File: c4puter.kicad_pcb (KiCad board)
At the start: 6 copper layers, 200 x 200 mm, 34 parts, among them J1 CONN-10018783-10202TLF-PCIEx8, J2 CONN-10018783-10202TLF-PCIEx8, J3 CONN-10018783-10202TLF-PCIEx8, J4 CONN-10018783-10202TLF-PCIEx8, J5 CONN-10018783-10202TLF-PCIEx8, J6 CONN-10018783-10202TLF-PCIEx8, J7 19V 3A, J8 DEBUG, U1 AOZ1037, U2 TSC101B

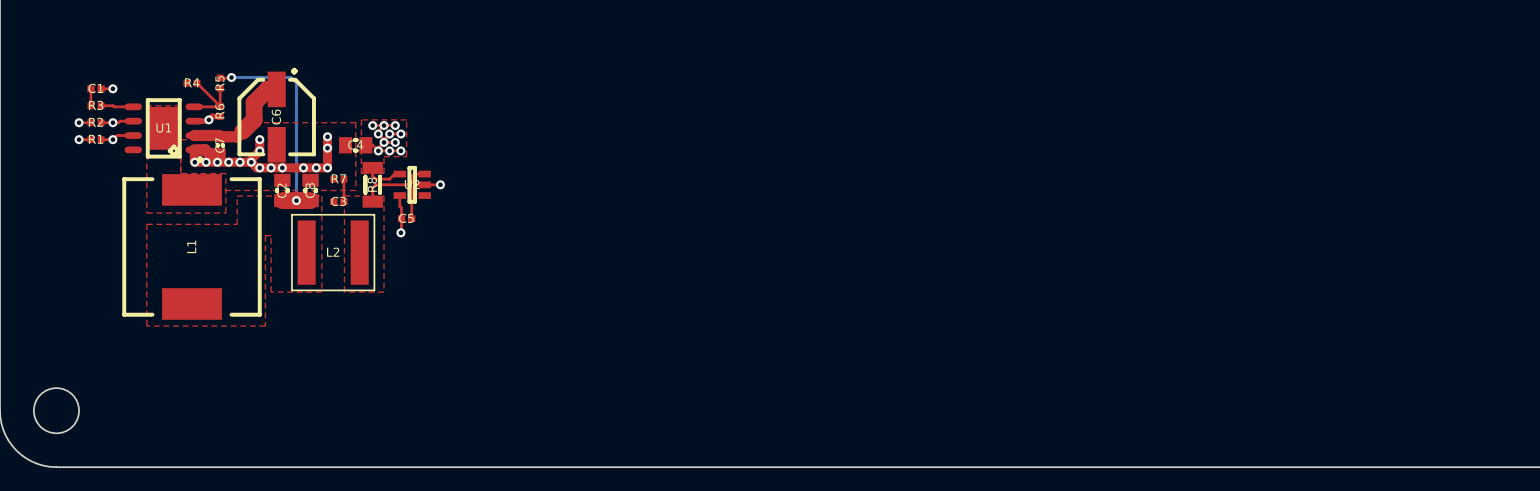
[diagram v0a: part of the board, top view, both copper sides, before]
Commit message: Finish power supplies
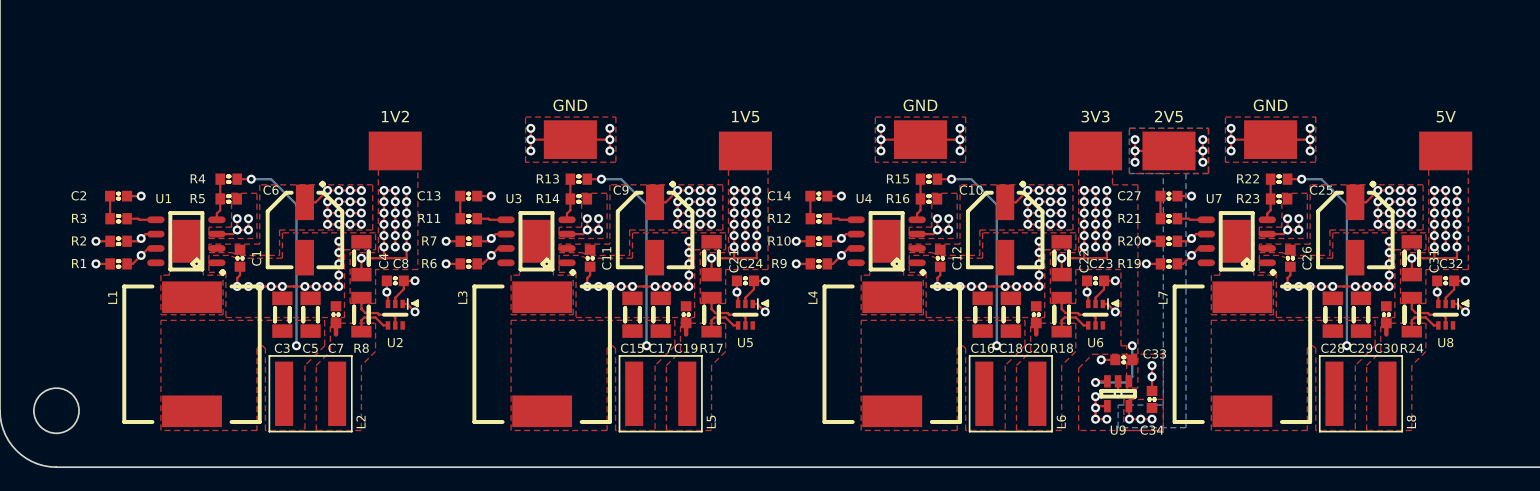
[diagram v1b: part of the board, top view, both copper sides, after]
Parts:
- added C10: 22u(P), IPC7351-Nominal:CAPAE660X570, F.Cu at (89.0, 179.0)
- added C11: 100n, IPC7351-Nominal:CAPC1608X55, F.Cu at (52.2, 181.5)
- added C12: 100n, IPC7351-Nominal:CAPC1608X55, F.Cu at (83.2, 181.5)
- added C13: 220p, IPC7351-Nominal:CAPC1608X55, F.Cu at (41.5, 176.0)
- added C14: 220p, IPC7351-Nominal:CAPC1608X55, F.Cu at (72.5, 176.0)
- added C15: 22u, IPC7351-Nominal:CAPC3216X70, F.Cu at (56.0, 186.5)
- added C16: 22u, IPC7351-Nominal:CAPC3216X70, F.Cu at (87.0, 186.5)
- added C17: 22u, IPC7351-Nominal:CAPC3216X70, F.Cu at (58.5, 186.5)
- added C18: 22u, IPC7351-Nominal:CAPC3216X70, F.Cu at (89.5, 186.5)
- added C19: 100n, IPC7351-Nominal:CAPC1608X55, F.Cu at (60.8, 186.5)
- added C20: 100n, IPC7351-Nominal:CAPC1608X55, F.Cu at (91.8, 186.5)
- added C21: 22u, IPC7351-Nominal:CAPC3216X70, F.Cu at (63.0, 181.5)
- added C22: 22u, IPC7351-Nominal:CAPC3216X70, F.Cu at (94.0, 181.5)
- added C23: 100n, IPC7351-Nominal:CAPC1608X55, F.Cu at (97.0, 183.5)
- added C24: 100n, IPC7351-Nominal:CAPC1608X55, F.Cu at (66.0, 183.5)
- added C25: 22u(P), IPC7351-Nominal:CAPAE660X570, F.Cu at (120.0, 179.0)
- added C26: 100n, IPC7351-Nominal:CAPC1608X55, F.Cu at (114.2, 181.5)
- added C27: 220p, IPC7351-Nominal:CAPC1608X55, F.Cu at (103.5, 176.0)
- added C28: 22u, IPC7351-Nominal:CAPC3216X70, F.Cu at (118.0, 186.5)
- added C29: 22u, IPC7351-Nominal:CAPC3216X70, F.Cu at (120.5, 186.5)
- added C30: 100n, IPC7351-Nominal:CAPC1608X55, F.Cu at (122.8, 186.5)
- added C31: 22u, IPC7351-Nominal:CAPC3216X70, F.Cu at (125.0, 181.5)
- added C32: 100n, IPC7351-Nominal:CAPC1608X55, F.Cu at (128.0, 183.5)
- added C33: 2u2, IPC7351-Nominal:CAPC1608X55, F.Cu at (99.5, 190.5)
- added C34: 2u2, IPC7351-Nominal:CAPC1608X55, F.Cu at (102.0, 194.0)
- added C9: 22u(P), IPC7351-Nominal:CAPAE660X570, F.Cu at (58.0, 179.0)
- added L3: 4u7, manuf:BOURNS-SRR1210, F.Cu at (48.0, 190.0)
- added L4: 10u, manuf:BOURNS-SRR1210, F.Cu at (79.0, 190.0)
- added L5: 2u2, manuf:MURATA-DG6050C, F.Cu at (58.5, 193.5)
- added L6: 2u2, manuf:MURATA-DG6050C, F.Cu at (89.5, 193.5)
- added L7: 10u, manuf:BOURNS-SRR1210, F.Cu at (110.0, 190.0)
- added L8: 2u2, manuf:MURATA-DG6050C, F.Cu at (120.5, 193.5)
- added R10: 100k, IPC7351-Nominal:RESC1608X50, F.Cu at (72.5, 180.0)
- added R11: 10k, IPC7351-Nominal:RESC1608X50, F.Cu at (41.5, 178.0)
- added R12: 10k, IPC7351-Nominal:RESC1608X50, F.Cu at (72.5, 178.0)
- added R13: 10k, IPC7351-Nominal:RESC1608X50, F.Cu at (51.2, 174.5)
- added R14: 10k, IPC7351-Nominal:RESC1608X50, F.Cu at (51.2, 176.2)
- added R15: 10k, IPC7351-Nominal:RESC1608X50, F.Cu at (82.2, 174.5)
- added R16: 10k, IPC7351-Nominal:RESC1608X50, F.Cu at (82.2, 176.2)
- added R17: 0R005, IPC7351-Nominal:RESC3216X60, F.Cu at (63.0, 186.5)
- added R18: 0R005, IPC7351-Nominal:RESC3216X60, F.Cu at (94.0, 186.5)
- added R19: 100k, IPC7351-Nominal:RESC1608X50, F.Cu at (103.5, 182.0)
- added R20: 100k, IPC7351-Nominal:RESC1608X50, F.Cu at (103.5, 180.0)
- added R21: 10k, IPC7351-Nominal:RESC1608X50, F.Cu at (103.5, 178.0)
- added R22: 10k, IPC7351-Nominal:RESC1608X50, F.Cu at (113.2, 174.5)
- added R23: 10k, IPC7351-Nominal:RESC1608X50, F.Cu at (113.2, 176.2)
- added R24: 0R005, IPC7351-Nominal:RESC3216X60, F.Cu at (125.0, 186.5)
- added R9: 100k, IPC7351-Nominal:RESC1608X50, F.Cu at (72.5, 182.0)
- added TP1: 1V2, manuf:TESTPOINT-KEYSTONE-5018, F.Cu at (35.0, 172.0)
- added TP2: 3V3, manuf:TESTPOINT-KEYSTONE-5018, F.Cu at (97.0, 172.0)
- added TP3: 1V5, manuf:TESTPOINT-KEYSTONE-5018, F.Cu at (66.0, 172.0)
- added TP4: 5V, manuf:TESTPOINT-KEYSTONE-5018, F.Cu at (128.0, 172.0)
- added TP5: 2V5, manuf:TESTPOINT-KEYSTONE-5018, F.Cu at (103.5, 172.0)
- added TP6: GND, manuf:TESTPOINT-KEYSTONE-5018, F.Cu at (50.5, 171.0)
- added TP7: GND, manuf:TESTPOINT-KEYSTONE-5018, F.Cu at (81.5, 171.0)
- added TP8: GND, manuf:TESTPOINT-KEYSTONE-5018, F.Cu at (112.5, 171.0)
- added U3: AOZ1037, IPC7351-Nominal:SOIC127P600X175-9, F.Cu at (47.5, 180.0)
- added U4: AOZ1037, IPC7351-Nominal:SOIC127P600X175-9, F.Cu at (78.5, 180.0)
- added U5: INA199, smd-semi:SC-70-6, F.Cu at (66.0, 186.5)
- added U6: INA199, smd-semi:SC-70-6, F.Cu at (97.0, 186.5)
- added U7: AOZ1037, IPC7351-Nominal:SOIC127P600X175-9, F.Cu at (109.5, 180.0)
- added U8: INA199, smd-semi:SC-70-6, F.Cu at (128.0, 186.5)
- added U9: TLV70225DBV, smd-semi:SOT-23-5, F.Cu at (99.0, 193.5)
- C1: value 220p -> 100n; footprint IPC7351-Nominal:CAPC1005X55 -> IPC7351-Nominal:CAPC1608X55
- C2: value 22u -> 220p; footprint IPC7351-Nominal:CAPC2012X70 -> IPC7351-Nominal:CAPC1608X55
- C3, C5: value 100n -> 22u; footprint IPC7351-Nominal:CAPC1005X55 -> IPC7351-Nominal:CAPC3216X70
- C4: footprint IPC7351-Nominal:CAPC2012X70 -> IPC7351-Nominal:CAPC3216X70
- C8: value 22u -> 100n; footprint IPC7351-Nominal:CAPC2012X70 -> IPC7351-Nominal:CAPC1608X55
- R1, R2, R3, R6: footprint IPC7351-Nominal:RESC1005X40 -> IPC7351-Nominal:RESC1608X50
- R4, R5: value 100k -> 10k; footprint IPC7351-Nominal:RESC1005X40 -> IPC7351-Nominal:RESC1608X50
- R7: value 47 -> 100k; footprint IPC7351-Nominal:RESC1005X40 -> IPC7351-Nominal:RESC1608X50
- R8: value 0R01 -> 0R005
- U2: value TSC101B -> INA199; footprint smd-semi:SOT-23-5 -> smd-semi:SC-70-6
- moved R6 25.8 mm to (41.5, 182.0), turned to 0 degrees
- moved C1 19.7 mm to (21.2, 181.5), turned to 270 degrees
- moved C7 18.2 mm to (29.8, 186.5), turned to 90 degrees
- moved C2 14.5 mm to (10.5, 176.0), turned to 0 degrees
- moved R7 12.7 mm to (41.5, 180.0), turned to 180 degrees
- moved L2 12.7 mm to (27.5, 193.5)
- moved C5 12.0 mm to (27.5, 186.5), turned to 90 degrees
- moved U2 11.6 mm to (35.0, 186.5), turned to 270 degrees
- moved R8 11.5 mm to (32.0, 186.5)
- moved C3 11.2 mm to (25.0, 186.5), turned to 90 degrees
- moved R1 11.2 mm to (10.5, 182.0), turned to 0 degrees
- moved C8 11.0 mm to (35.0, 183.5), turned to 0 degrees
- moved R2 10.7 mm to (10.5, 180.0), turned to 180 degrees
- moved C6 10.3 mm to (27.0, 179.0)
- moved R5 10.3 mm to (20.2, 176.2), turned to 180 degrees
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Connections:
- C1 pad 1: Net-(C1-Pad1) -> +12
- C2 pad 1: /Power/RAW1V2 -> Net-(C2-Pad1)
- C3 pad 1: Net-(C3-Pad1) -> /Power/RAW1V2
- C3 pad 2: /Power/S+1V2 -> GND
- C5 pad 1: GND -> /Power/RAW1V2
- C5 pad 2: +3.3SB -> GND
- C7 pad 1: +12 -> /Power/S+1V2
- C8 pad 1: /Power/RAW1V2 -> +3.3SB
- R1 pad 1: /Power/PG1V2 -> +3.3SB
- R1 pad 2: +3.3SB -> /Power/PG1V2
- R2 pad 1: GND -> /Power/EN1V2
- R2 pad 2: /Power/EN1V2 -> GND
- R3 pad 2: Net-(C1-Pad1) -> Net-(C2-Pad1)
- R4 pad 1: /Power/TRIM1V2 -> Net-(R4-Pad1)
- R4 pad 2: Net-(R4-Pad2) -> /Power/RAW1V2
- R5 pad 1: Net-(R4-Pad2) -> GND
- R5 pad 2: /Power/RAW1V2 -> Net-(R4-Pad1)
- R6 pad 1: GND -> +3.3SB
- R6 pad 2: Net-(R4-Pad2) -> /Power/PG1V5
- R7 pad 1: GND -> /Power/EN1V5
- R7 pad 2: Net-(C3-Pad1) -> GND
- U1 pad 4: Net-(R4-Pad2) -> Net-(R4-Pad1)
- U2 pad 1: /Power/IMON1V2 -> GND
- U2 pad 3: /Power/S+1V2 -> +3.3SB
- U2 pad 4: /Power/1V2 -> /Power/S+1V2
- U2 pad 5: +3.3SB -> /Power/1V2
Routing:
- net GND: track 609.4 -> 729.4 mm, vias 57 -> 147
- net +12: track 9.97 -> 69.7 mm, vias 0 -> 64
- net /Power/3V3: track 0.00 -> 35.8 mm, vias 0 -> 21
- net /Power/1V5: track 0.00 -> 28.5 mm, vias 0 -> 19
- net /Power/5V: track 0.00 -> 28.5 mm, vias 0 -> 19
- net /Power/RAW5V: track 0.00 -> 18.7 mm, vias 0 -> 2
- net /Power/RAW3V3: track 0.00 -> 18.7 mm, vias 0 -> 2
- net /Power/RAW1V5: track 0.00 -> 18.7 mm, vias 0 -> 2
- net /Power/1V2: track 14.3 -> 28.5 mm, vias 11 -> 19
- net /Power/2V5: track 0.00 -> 13.2 mm, vias 0 -> 9
- net +3.3SB: track 4.43 -> 13.4 mm, vias 2 -> 8
- net Net-(R4-Pad2): track 6.82 -> 0.00 mm
- net /Power/S+5V: track 0.00 -> 4.74 mm
- net /Power/S+3V3: track 0.00 -> 4.74 mm
- net /Power/S+1V5: track 0.00 -> 4.74 mm
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- added copper zone on F.Cu, net +12
- added copper zone on F.Cu, net /Power/1V5
- added copper zone on B.Cu, net /Power/2V5
- added copper zone on F.Cu, net /Power/2V5
- added copper zone on F.Cu, net /Power/3V3
- added copper zone on F.Cu, net /Power/5V
- added copper zone on F.Cu, net /Power/RAW1V5
- added copper zone on F.Cu, net /Power/RAW3V3
- added copper zone on F.Cu, net /Power/RAW5V
- added copper zone on F.Cu, net /Power/S+1V5
- added copper zone on F.Cu, net /Power/S+3V3
- added copper zone on F.Cu, net /Power/S+5V
- added copper zone on F.Cu, net /Power/SW1V5
- added copper zone on F.Cu, net /Power/SW3V3
- added copper zone on F.Cu, net /Power/SW5V
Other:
- net class Default: clearance 0.1016 -> 0.2; trace_width 0.1016 -> 0.2; via_dia 0.48 -> 0.8; via_drill 0.2 -> 0.4
- net class Tight added: clearance 0.1016, trace_width 0.1016, via_dia 0.48, via_drill 0.2
- rule trace_clearance: 0.1016 -> 0.2

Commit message: Upgrade FPGA size, re-route SDRAM
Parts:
- removed J5, J6: CONN-10018783-10202TLF-PCIEx8, conn-fci:CONN-10018783-10202TLF-PCIEx8-FCI
- BRIDGE1: value XC6SLX25-CSG324 -> XC6SLX25-FGG484; footprint manuf:XILINX-CSG324 -> manuf:XILINX-FGG484
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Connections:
- net /Multibridge/CPU4 renamed Net-(BRIDGE1-PadU15)
- net /Multibridge/CPU5 renamed Net-(BRIDGE1-PadV15)
- BRIDGE1 pad A10: /Multibridge/DQ56 -> /Multibridge/DQS4_N
- BRIDGE1 pad A11: /Multibridge/DM7 -> /Multibridge/DQS5_N
- BRIDGE1 pad A12: /Multibridge/DQ59 -> /Multibridge/DQ35
- BRIDGE1 pad A13: /Multibridge/SA1 -> VDDRREF
- BRIDGE1 pad A14: VREF -> /Multibridge/DQ41
- BRIDGE1 pad A15: Net-(BRIDGE1-PadA15) -> /Multibridge/DQ42
- BRIDGE1 pad A16: Net-(BRIDGE1-PadA16) -> /Multibridge/DQ43
- BRIDGE1 pad A17: /Power Distrib/BR_TCK -> /Multibridge/DQ49
- BRIDGE1 pad A18: GND -> /Multibridge/DQS6_N
- BRIDGE1 pad A2: /Multibridge/DQS4_N -> /Multibridge/A10
- BRIDGE1 pad A3: /Multibridge/DQ34 -> /Multibridge/~WE
- BRIDGE1 pad A4: /Multibridge/DQ40 -> VDDRREF
- BRIDGE1 pad A5: /Multibridge/DM5 -> /Multibridge/~CAS
- BRIDGE1 pad A6: VREF -> /Multibridge/~S1
- BRIDGE1 pad A7: /Multibridge/DQ48 -> /Multibridge/DQ32
- BRIDGE1 pad A8: /Multibridge/DQS6_N -> Net-(BRIDGE1-PadA8)
- BRIDGE1 pad A9: /Multibridge/DQ50 -> VDDRREF
- BRIDGE1 pad B1: +3.3 -> /Multibridge/CK0_N
- BRIDGE1 pad B10: +1.5 -> /Multibridge/DQS4_P
- BRIDGE1 pad B11: /Multibridge/DQ58 -> VRAM
- BRIDGE1 pad B12: /Multibridge/SA0 -> /Multibridge/DQ40
- BRIDGE1 pad B14: /Multibridge/DQ63 -> /Multibridge/DM5
- BRIDGE1 pad B15: +1.5 -> VRAM
- BRIDGE1 pad B16: Net-(BRIDGE1-PadB16) -> /Multibridge/DQ48
- BRIDGE1 pad B17: +3.3 -> GND
- BRIDGE1 pad B18: /Power Distrib/BR_TMS -> /Multibridge/DQS6_P
- BRIDGE1 pad B2: /Multibridge/DQS4_P -> /Multibridge/CK0_P
- BRIDGE1 pad B3: /Multibridge/DQ35 -> VDDRREF
- BRIDGE1 pad B4: /Multibridge/DQ41 -> VRAM
- BRIDGE1 pad B5: +1.5 -> GND
- BRIDGE1 pad B6: /Multibridge/DQ43 -> /Multibridge/A13
- BRIDGE1 pad B7: GND -> VRAM
- BRIDGE1 pad B8: /Multibridge/DQS6_P -> /Multibridge/DQ33
- BRIDGE1 pad B9: /Multibridge/DQ51 -> GND
- BRIDGE1 pad C1: VREF -> /Multibridge/CK1_N
- BRIDGE1 pad C10: /Multibridge/DQ57 -> /Multibridge/DQ44
- BRIDGE1 pad C11: /Multibridge/DQ54 -> /Multibridge/DQS5_P
- BRIDGE1 pad C12: /Multibridge/DQ60 -> /Multibridge/DQ46
- BRIDGE1 pad C14: /Multibridge/DQS7_N -> /Multibridge/DQ52
- BRIDGE1 pad C15: /Multibridge/DQ62 -> /Multibridge/DM6
- BRIDGE1 pad C16: GND -> VDDRREF
- BRIDGE1 pad C17: /Multibridge/CD2 -> /Multibridge/DQ55
- BRIDGE1 pad C18: /Multibridge/CD3 -> /Power Distrib/BR_TMS
- BRIDGE1 pad C2: /Multibridge/DQ33 -> VRAM
- BRIDGE1 pad C3: GND -> /Multibridge/CK1_P
- BRIDGE1 pad C4: VREF -> (no net)
- BRIDGE1 pad C5: /Multibridge/DQ42 -> /Multibridge/BA1
- BRIDGE1 pad C6: Net-(BRIDGE1-PadC6) -> /Multibridge/~RAS
- BRIDGE1 pad C7: /Multibridge/DQ49 -> /Multibridge/ODT0
- BRIDGE1 pad C8: /Multibridge/DQ44 -> /Multibridge/DQ36
- BRIDGE1 pad C9: /Multibridge/DQS5_N -> /Multibridge/DM4
- BRIDGE1 pad D1: /Multibridge/~S1 -> /Multibridge/A3
- BRIDGE1 pad D10: GND -> /Multibridge/DQ45
- BRIDGE1 pad D11: Net-(BRIDGE1-PadD11) -> /Multibridge/DQ34
- BRIDGE1 pad D12: /Multibridge/DQ61 -> /Multibridge/DQ47
- BRIDGE1 pad D13: +1.5 -> /Multibridge/DQS7_N
- BRIDGE1 pad D14: /Multibridge/DQS7_P -> /Multibridge/DQ53
- BRIDGE1 pad D15: /Power Distrib/BR_TDI -> /Multibridge/DQ54
- BRIDGE1 pad D16: /Power Distrib/BR_TDO -> VCCAUX
- BRIDGE1 pad D17: /Multibridge/CD6 -> /Multibridge/DQ60
- BRIDGE1 pad D18: /Multibridge/CD7 -> GND
- BRIDGE1 pad D2: /Multibridge/DQ32 -> /Multibridge/A1
- BRIDGE1 pad D3: /Multibridge/ODT0 -> (no net)
- BRIDGE1 pad D4: /Multibridge/ODT1 -> GND
- BRIDGE1 pad D5: GND -> (no net)
- BRIDGE1 pad D6: /Multibridge/DQ38 -> /Multibridge/~S0
- BRIDGE1 pad D7: +1.5 -> /Multibridge/ODT1
- BRIDGE1 pad D8: /Multibridge/DQ39 -> /Multibridge/DQ37
- BRIDGE1 pad D9: /Multibridge/DQS5_P -> /Multibridge/DQ38
- BRIDGE1 pad E1: /Multibridge/~CAS -> /Multibridge/A5
- BRIDGE1 pad E10: +1.5 -> (no net)
- BRIDGE1 pad E11: Net-(BRIDGE1-PadE11) -> GND
- BRIDGE1 pad E12: /Multibridge/DM6 -> Net-(BRIDGE1-PadE12)
- BRIDGE1 pad E13: /Multibridge/DQ55 -> VRAM
- BRIDGE1 pad E14: +3.3 -> /Multibridge/DM7
- BRIDGE1 pad E16: /Multibridge/CD10 -> /Multibridge/DQ63
- BRIDGE1 pad E17: Net-(BRIDGE1-PadE17) -> VRAM
- BRIDGE1 pad E18: /Multibridge/CD11 -> /Power Distrib/BR_TDI
- BRIDGE1 pad E2: +1.5 -> GND
- BRIDGE1 pad E3: /Multibridge/A13 -> /Multibridge/A0
- BRIDGE1 pad E4: /Multibridge/~RAS -> (no net)
- BRIDGE1 pad E5: +3.3 -> (no net)
- BRIDGE1 pad E6: Net-(BRIDGE1-PadE6) -> (no net)
- BRIDGE1 pad E7: Net-(BRIDGE1-PadE7) -> GND
- BRIDGE1 pad E8: Net-(BRIDGE1-PadE8) -> (no net)
- BRIDGE1 pad E9: +3.3 -> VRAM
- BRIDGE1 pad F1: /Multibridge/A10 -> /Multibridge/A9
- BRIDGE1 pad F10: /Multibridge/DQ46 -> (no net)
- BRIDGE1 pad F11: /Multibridge/DQ52 -> VCCAUX
- BRIDGE1 pad F12: /Multibridge/DQ53 -> /Multibridge/DQ61
- BRIDGE1 pad F13: Net-(BRIDGE1-PadF13) -> /Multibridge/DQS7_P
- BRIDGE1 pad F14: /Multibridge/CD4 -> /Multibridge/DQ59
- BRIDGE1 pad F15: /Multibridge/CD0 -> /Multibridge/SA0
- BRIDGE1 pad F16: /Multibridge/CD1 -> (no net)
- BRIDGE1 pad F17: /Multibridge/CD14 -> (no net)
- BRIDGE1 pad F18: /Multibridge/CD15 -> Net-(BRIDGE1-PadF18)
- BRIDGE1 pad F2: /Multibridge/~WE -> /Multibridge/A8
- BRIDGE1 pad F3: /Multibridge/BA1 -> /Multibridge/A2
- BRIDGE1 pad F4: /Multibridge/~S0 -> VRAM
- BRIDGE1 pad F5: /Multibridge/DQ36 -> /Multibridge/DQ50
- BRIDGE1 pad F6: /Multibridge/DQ37 -> VRAM
- BRIDGE1 pad F7: Net-(BRIDGE1-PadF7) -> (no net)
- BRIDGE1 pad F8: Net-(BRIDGE1-PadF8) -> (no net)
- BRIDGE1 pad F9: VREF -> (no net)
- BRIDGE1 pad G1: /Multibridge/CK0_N -> /Multibridge/A12
- BRIDGE1 pad G10: +3.3 -> VRAM
- BRIDGE1 pad G11: /Multibridge/DQ47 -> (no net)
- BRIDGE1 pad G12: GND -> VCCAUX
- BRIDGE1 pad G13: /Multibridge/CD9 -> /Multibridge/DQ58
- BRIDGE1 pad G14: /Multibridge/CD5 -> VRAM
- BRIDGE1 pad G15: Net-(BRIDGE1-PadG15) -> /Power Distrib/BR_TCK
- BRIDGE1 pad G16: /Multibridge/CD20 -> (no net)
- BRIDGE1 pad G17: GND -> (no net)
- BRIDGE1 pad G18: /Multibridge/CD21 -> GND
- BRIDGE1 pad G2: GND -> VRAM
- BRIDGE1 pad G3: /Multibridge/CK0_P -> /Multibridge/A6
- BRIDGE1 pad G4: +1.5 -> /Multibridge/A4
- BRIDGE1 pad G6: /Multibridge/DM4 -> /Multibridge/DQ51
- BRIDGE1 pad G7: +1.2 -> (no net)
- BRIDGE1 pad G8: Net-(BRIDGE1-PadG8) -> (no net)
- BRIDGE1 pad G9: /Multibridge/DQ45 -> (no net)
- BRIDGE1 pad H1: /Multibridge/A1 -> /Multibridge/CKE0
- BRIDGE1 pad H10: GND -> (no net)
- BRIDGE1 pad H11: +1.2 -> (no net)
- BRIDGE1 pad H12: /Multibridge/CD8 -> /Multibridge/DQ56
- BRIDGE1 pad H13: /Multibridge/CD16 -> /Multibridge/DQ62
- BRIDGE1 pad H14: /Multibridge/CD17 -> /Multibridge/SA1
- BRIDGE1 pad H15: /Multibridge/CD18 -> VCCAUX
- BRIDGE1 pad H16: /Multibridge/CD19 -> (no net)
- BRIDGE1 pad H17: /Multibridge/CD30 -> (no net)
- BRIDGE1 pad H18: /Multibridge/CD31 -> Net-(BRIDGE1-PadH18)
- BRIDGE1 pad H2: /Multibridge/A3 -> /Multibridge/BA2
- BRIDGE1 pad H3: /Multibridge/CK1_N -> /Multibridge/A11
- BRIDGE1 pad H4: /Multibridge/CK1_P -> /Multibridge/A7
- BRIDGE1 pad H5: /Multibridge/A0 -> /Multibridge/DQ7
- BRIDGE1 pad H6: /Multibridge/A2 -> /Multibridge/DQ12
- BRIDGE1 pad H7: Net-(BRIDGE1-PadH7) -> GND
- BRIDGE1 pad H8: GND -> /Multibridge/DQ13
- BRIDGE1 pad H9: +1.2 -> VCCAUX
- BRIDGE1 pad J1: /Multibridge/A5 -> /Multibridge/DQ27
- BRIDGE1 pad J10: +1.2 -> VCORE
- BRIDGE1 pad J12: +3.3 -> VCORE
- BRIDGE1 pad J13: /Multibridge/CD22 -> GND
- BRIDGE1 pad J14: Net-(BRIDGE1-PadJ14) -> VCORE
- BRIDGE1 pad J16: /Multibridge/CD_CLK -> (no net)
- BRIDGE1 pad J18: /Multibridge/CD_~ADH -> VCCO1
- BRIDGE1 pad J2: +1.5 -> GND
- BRIDGE1 pad J3: /Multibridge/A8 -> /Multibridge/A15
- BRIDGE1 pad J4: GND -> /Multibridge/A14
- BRIDGE1 pad J5: +1.5 -> VRAM
- BRIDGE1 pad J6: /Multibridge/A4 -> /Multibridge/DQS0_N
- BRIDGE1 pad J7: Net-(BRIDGE1-PadJ7) -> /Multibridge/DQ6
- BRIDGE1 pad J8: +1.2 -> VCORE
- BRIDGE1 pad K1: /Multibridge/A9 -> /Multibridge/DM3
- BRIDGE1 pad K11: +1.2 -> VCORE
- BRIDGE1 pad K12: /Multibridge/CD12 -> GND
- BRIDGE1 pad K13: /Multibridge/CD13 -> VCORE
- BRIDGE1 pad K14: /Multibridge/CD23 -> GND
- BRIDGE1 pad K15: /Multibridge/CD26 -> VCCAUX
- BRIDGE1 pad K16: /Multibridge/CD27 -> (no net)
- BRIDGE1 pad K17: /Multibridge/CD_~ADL -> Net-(BRIDGE1-PadK17)
- BRIDGE1 pad K18: /Multibridge/CD_R/~W -> Net-(BRIDGE1-PadK18)
- BRIDGE1 pad K2: /Multibridge/A12 -> /Multibridge/DQ26
- BRIDGE1 pad K3: /Multibridge/A6 -> /Multibridge/DQ31
- BRIDGE1 pad K4: /Multibridge/A7 -> /Multibridge/CKE1
- BRIDGE1 pad K5: /Multibridge/A11 -> /Multibridge/DQ5
- BRIDGE1 pad K6: Net-(BRIDGE1-PadK6) -> /Multibridge/DQS0_P
- BRIDGE1 pad K7: +3.3 -> (no net)
- BRIDGE1 pad K8: GND -> (no net)
- BRIDGE1 pad K9: +1.2 -> VCORE
- BRIDGE1 pad L1: /Multibridge/BA2 -> /Multibridge/DQ25
- BRIDGE1 pad L10: +1.2 -> VCORE
- BRIDGE1 pad L12: /Multibridge/CD24 -> VCORE
- BRIDGE1 pad L13: /Multibridge/CD25 -> GND
- BRIDGE1 pad L14: Net-(BRIDGE1-PadL14) -> VCORE
- BRIDGE1 pad L15: /Multibridge/CD28 -> (no net)
- BRIDGE1 pad L16: /Multibridge/CD29 -> VCCO1
- BRIDGE1 pad L17: /Multibridge/CD_SCLK -> Net-(BRIDGE1-PadL17)
- BRIDGE1 pad L18: /Multibridge/CD_MOSI -> GND
- BRIDGE1 pad L2: /Multibridge/CKE0 -> VRAM
- BRIDGE1 pad L3: /Multibridge/A14 -> /Multibridge/DQ30
- BRIDGE1 pad L4: /Multibridge/A15 -> /Multibridge/DQS3_N
- BRIDGE1 pad L5: Net-(BRIDGE1-PadL5) -> GND
- BRIDGE1 pad L6: Net-(BRIDGE1-PadL6) -> (no net)
- BRIDGE1 pad L7: Net-(BRIDGE1-PadL7) -> VRAM
- BRIDGE1 pad L8: +1.2 -> VCCAUX
- BRIDGE1 pad M1: /Multibridge/DQ27 -> /Multibridge/DQ19
- BRIDGE1 pad M10: /Multibridge/CPU14 -> GND
- BRIDGE1 pad M11: /Multibridge/CPU10 -> VCORE
- BRIDGE1 pad M12: +1.2 -> GND
- BRIDGE1 pad M13: Net-(BRIDGE1-PadM13) -> VCORE
- BRIDGE1 pad M14: Net-(BRIDGE1-PadM14) -> GND
- BRIDGE1 pad M15: Net-(BRIDGE1-PadM15) -> VCCAUX
- BRIDGE1 pad M16: /Multibridge/CD_MISO -> (no net)
- BRIDGE1 pad M17: GND -> (no net)
- BRIDGE1 pad M18: /Multibridge/CD_~SS0 -> (no net)
- BRIDGE1 pad M2: GND -> /Multibridge/DQ24
- BRIDGE1 pad M3: /Multibridge/CKE1 -> /Multibridge/DQS3_P
- BRIDGE1 pad M4: +1.5 -> VDDRREF
- BRIDGE1 pad M5: VREF -> /Multibridge/DQ28
- BRIDGE1 pad M6: GND -> (no net)
- BRIDGE1 pad M7: +1.2 -> (no net)
- BRIDGE1 pad M8: /Multibridge/CPUnW -> (no net)
- BRIDGE1 pad M9: +3.3 -> VCORE
- BRIDGE1 pad N1: /Multibridge/DQ26 -> /Multibridge/DQ18
- BRIDGE1 pad N10: /Multibridge/CPU13 -> VCORE
- BRIDGE1 pad N11: /Multibridge/CPU11 -> GND
- BRIDGE1 pad N12: /Multibridge/CPU8 -> VCORE
- BRIDGE1 pad N14: Net-(BRIDGE1-PadN14) -> VCORE
- BRIDGE1 pad N15: /Multibridge/CD_~SS5 -> /Power Distrib/BR_SUSP
- BRIDGE1 pad N16: Net-(BRIDGE1-PadN16) -> (no net)
- BRIDGE1 pad N17: /Multibridge/CD_~SS1 -> GND
- BRIDGE1 pad N18: /Multibridge/CD_~SS2 -> VCCO1
- BRIDGE1 pad N2: /Multibridge/DM3 -> GND
- BRIDGE1 pad N3: VREF -> /Multibridge/DQ29
- BRIDGE1 pad N4: /Multibridge/DQ31 -> (no net)
- BRIDGE1 pad N5: /Multibridge/DQ30 -> VRAM
- BRIDGE1 pad N6: /Multibridge/DQ15 -> (no net)
- BRIDGE1 pad N7: /Multibridge/CPUASTR -> (no net)
- BRIDGE1 pad N8: /Multibridge/CPUCLK -> VCCAUX
- BRIDGE1 pad N9: /Multibridge/CPU15 -> GND
- BRIDGE1 pad P1: /Multibridge/DQ25 -> /Multibridge/DQS2_N
- BRIDGE1 pad P10: +3.3 -> GND
- BRIDGE1 pad P11: /Multibridge/DQ6 -> VCORE
- BRIDGE1 pad P12: /Multibridge/CPU9 -> GND
- BRIDGE1 pad P13: Net-(BRIDGE1-PadP13) -> VCORE
- BRIDGE1 pad P14: +3.3 -> GND
- BRIDGE1 pad P15: Net-(BRIDGE1-PadP15) -> (no net)
- BRIDGE1 pad P16: Net-(BRIDGE1-PadP16) -> (no net)
- BRIDGE1 pad P17: /Multibridge/CD_~SS3 -> (no net)
- BRIDGE1 pad P18: /Multibridge/CD_~SS4 -> (no net)
- BRIDGE1 pad P2: /Multibridge/DQ24 -> /Multibridge/DQS2_P
- BRIDGE1 pad P3: Net-(BRIDGE1-PadP3) -> (no net)
- BRIDGE1 pad P4: Net-(BRIDGE1-PadP4) -> (no net)
- BRIDGE1 pad P5: +3.3 -> (no net)
- BRIDGE1 pad P6: /Multibridge/DQ23 -> (no net)
- BRIDGE1 pad P7: /Multibridge/DQ20 -> (no net)
- BRIDGE1 pad P8: /Multibridge/CPUDSTR -> (no net)
- BRIDGE1 pad P9: +1.5 -> VCORE
- BRIDGE1 pad R1: GND -> /Multibridge/DQ17
- BRIDGE1 pad R10: /Multibridge/DQ12 -> VCCAUX
- BRIDGE1 pad R11: /Multibridge/DQ7 -> Net-(BRIDGE1-PadR11)
- BRIDGE1 pad R12: +1.5 -> VCCAUX
- BRIDGE1 pad R13: /Multibridge/DQS0_P -> (no net)
- BRIDGE1 pad R14: GND -> VCORE
- BRIDGE1 pad R15: /Multibridge/CPU0 -> (no net)
- BRIDGE1 pad R16: /Power Distrib/BR_SUSP -> (no net)
- BRIDGE1 pad R17: Net-(BRIDGE1-PadR17) -> (no net)
- BRIDGE1 pad R2: +1.5 -> VRAM
- BRIDGE1 pad R3: /Multibridge/DQS3_P -> /Multibridge/DQ23
- BRIDGE1 pad R4: GND -> (no net)
- BRIDGE1 pad R5: /Multibridge/DQ28 -> GND
- BRIDGE1 pad R6: +1.5 -> VCCAUX
- BRIDGE1 pad R7: /Multibridge/DQ21 -> /Multibridge/DQ3
- BRIDGE1 pad R8: /Multibridge/SDRAM_~RST -> /Multibridge/DQ4
- BRIDGE1 pad R9: GND -> Net-(BRIDGE1-PadR9)
- BRIDGE1 pad T1: /Multibridge/DQ18 -> /Multibridge/DQ16
- BRIDGE1 pad T10: /Multibridge/DQ13 -> (no net)
- BRIDGE1 pad T11: VREF -> Net-(BRIDGE1-PadT11)
- BRIDGE1 pad T12: /Multibridge/CPU12 -> (no net)
- BRIDGE1 pad T13: /Multibridge/DQS0_N -> VRAM
- BRIDGE1 pad T14: /Multibridge/CPU6 -> (no net)
- BRIDGE1 pad T15: /Multibridge/CPU1 -> (no net)
- BRIDGE1 pad T16: GND -> (no net)
- BRIDGE1 pad T17: Net-(BRIDGE1-PadT17) -> (no net)
- BRIDGE1 pad T18: Net-(BRIDGE1-PadT18) -> (no net)
- BRIDGE1 pad T2: /Multibridge/DQ19 -> /Multibridge/DQ11
- BRIDGE1 pad T3: /Multibridge/DQS3_N -> /Multibridge/DM2
- BRIDGE1 pad T4: /Multibridge/DQ29 -> /Multibridge/DQ22
- BRIDGE1 pad T5: VREF -> Net-(BRIDGE1-PadT5)
- BRIDGE1 pad T6: /Multibridge/DQ22 -> Net-(BRIDGE1-PadT6)
- BRIDGE1 pad T7: /Multibridge/DM2 -> /Multibridge/DQ2
- BRIDGE1 pad T8: /Multibridge/DQ14 -> (no net)
- BRIDGE1 pad T9: /Multibridge/DM1 -> VRAM
- BRIDGE1 pad U1: /Multibridge/DQS2_N -> /Multibridge/DQ10
- BRIDGE1 pad U10: /Multibridge/DQ2 -> (no net)
- BRIDGE1 pad U11: /Multibridge/DQ1 -> VCCAUX
- BRIDGE1 pad U12: GND -> (no net)
- BRIDGE1 pad U13: /Multibridge/DQ4 -> Net-(BRIDGE1-PadU13)
- BRIDGE1 pad U14: +1.5 -> Net-(BRIDGE1-PadU14)
- BRIDGE1 pad U16: /Multibridge/CPU2 -> (no net)
- BRIDGE1 pad U17: Net-(BRIDGE1-PadU17) -> (no net)
- BRIDGE1 pad U18: Net-(BRIDGE1-PadU18) -> VCCO1
- BRIDGE1 pad U2: /Multibridge/DQS2_P -> GND
- BRIDGE1 pad U3: Net-(BRIDGE1-PadU3) -> /Multibridge/DQ20
- BRIDGE1 pad U4: +1.5 -> /Multibridge/DQ21
- BRIDGE1 pad U5: /Multibridge/DQ16 -> VRAM
- BRIDGE1 pad U6: GND -> /Multibridge/DM0
- BRIDGE1 pad U7: /Multibridge/DQS1_P -> GND
- BRIDGE1 pad U8: /Multibridge/DQ9 -> (no net)
- BRIDGE1 pad U9: +1.5 -> Net-(BRIDGE1-PadU9)
- BRIDGE1 pad V1: GND -> /Multibridge/DQS1_N
- BRIDGE1 pad V10: /Multibridge/DQ3 -> GND
- BRIDGE1 pad V11: /Multibridge/DM0 -> Net-(BRIDGE1-PadV11)
- BRIDGE1 pad V12: /Multibridge/DQ0 -> VRAM
- BRIDGE1 pad V13: /Multibridge/DQ5 -> Net-(BRIDGE1-PadV13)
- BRIDGE1 pad V14: /Multibridge/CPU7 -> GND
- BRIDGE1 pad V16: /Multibridge/CPU3 -> VRAM
- BRIDGE1 pad V17: Net-(BRIDGE1-PadV17) -> (no net)
- BRIDGE1 pad V18: GND -> (no net)
- BRIDGE1 pad V2: Net-(BRIDGE1-PadV2) -> /Multibridge/DQS1_P
- BRIDGE1 pad V3: Net-(BRIDGE1-PadV3) -> /Multibridge/DQ15
- BRIDGE1 pad V4: /Multibridge/DQ17 -> GND
- BRIDGE1 pad V5: /Multibridge/DQ11 -> /Multibridge/DQ0
- BRIDGE1 pad V6: /Multibridge/DQ10 -> VCCAUX
- BRIDGE1 pad V7: /Multibridge/DQS1_N -> Net-(BRIDGE1-PadV7)
- BRIDGE1 pad V8: VREF -> VRAM
- BRIDGE1 pad V9: /Multibridge/DQ8 -> Net-(BRIDGE1-PadV9)
- J1 pad A12: /Multibridge/CD1 -> /PerBus/D1
- J1 pad A14: /Multibridge/CD3 -> /PerBus/D3
- J1 pad A16: /Multibridge/CD5 -> /PerBus/D5
- J1 pad A18: /Multibridge/CD7 -> /PerBus/D7
- J1 pad A20: /Multibridge/CD9 -> /PerBus/D9
- J1 pad A22: /Multibridge/CD11 -> /PerBus/D11
- J1 pad A24: /Multibridge/CD13 -> /PerBus/D13
- J1 pad A26: /Multibridge/CD15 -> /PerBus/D15
- J1 pad A28: /Multibridge/CD17 -> /PerBus/D17
- J1 pad A30: /Multibridge/CD19 -> /PerBus/D19
- J1 pad A32: /Multibridge/CD21 -> /PerBus/D21
- J1 pad A34: /Multibridge/CD23 -> /PerBus/D23
- J1 pad A36: /Multibridge/CD25 -> /PerBus/D25
- J1 pad A38: /Multibridge/CD27 -> /PerBus/D27
- J1 pad A40: /Multibridge/CD29 -> /PerBus/D29
- J1 pad A42: /Multibridge/CD31 -> /PerBus/D31
- J1 pad A44: /Multibridge/CD_~ADH -> /PerBus/~ADH
- J1 pad A46: /Multibridge/CD_~SS0 -> /PerBus/~SS0
- J1 pad A48: /Multibridge/CD_R/~W -> /PerBus/R/~W
- J1 pad A5: /Multibridge/CD_SCLK -> /PerBus/SER_CLK
- J1 pad A6: /Multibridge/CD_MOSI -> /PerBus/SER_MOSI
- J1 pad A7: /Multibridge/CD_MISO -> /PerBus/SER_MISO
- J1 pad B12: /Multibridge/CD0 -> /PerBus/D0
- J1 pad B14: /Multibridge/CD2 -> /PerBus/D2
- J1 pad B16: /Multibridge/CD4 -> /PerBus/D4
- J1 pad B18: /Multibridge/CD6 -> /PerBus/D6
- J1 pad B20: /Multibridge/CD8 -> /PerBus/D8
- J1 pad B22: /Multibridge/CD10 -> /PerBus/D10
- J1 pad B24: /Multibridge/CD12 -> /PerBus/D12
- J1 pad B26: /Multibridge/CD14 -> /PerBus/D14
- J1 pad B28: /Multibridge/CD16 -> /PerBus/D16
- J1 pad B30: /Multibridge/CD18 -> /PerBus/D18
- J1 pad B32: /Multibridge/CD20 -> /PerBus/D20
- J1 pad B34: /Multibridge/CD22 -> /PerBus/D22
- J1 pad B36: /Multibridge/CD24 -> /PerBus/D24
- J1 pad B38: /Multibridge/CD26 -> /PerBus/D26
- J1 pad B40: /Multibridge/CD28 -> /PerBus/D28
- J1 pad B42: /Multibridge/CD30 -> /PerBus/D30
- J1 pad B44: /Multibridge/CD_CLK -> /PerBus/CLK
- J1 pad B46: /Multibridge/CD_~ADL -> /PerBus/~ADL
- J2 pad A12: /Multibridge/CD1 -> /PerBus/D1
- J2 pad A14: /Multibridge/CD3 -> /PerBus/D3
- J2 pad A16: /Multibridge/CD5 -> /PerBus/D5
- J2 pad A18: /Multibridge/CD7 -> /PerBus/D7
- J2 pad A20: /Multibridge/CD9 -> /PerBus/D9
- J2 pad A22: /Multibridge/CD11 -> /PerBus/D11
- J2 pad A24: /Multibridge/CD13 -> /PerBus/D13
- J2 pad A26: /Multibridge/CD15 -> /PerBus/D15
- J2 pad A28: /Multibridge/CD17 -> /PerBus/D17
- J2 pad A30: /Multibridge/CD19 -> /PerBus/D19
- J2 pad A32: /Multibridge/CD21 -> /PerBus/D21
- J2 pad A34: /Multibridge/CD23 -> /PerBus/D23
- J2 pad A36: /Multibridge/CD25 -> /PerBus/D25
- J2 pad A38: /Multibridge/CD27 -> /PerBus/D27
- J2 pad A40: /Multibridge/CD29 -> /PerBus/D29
- J2 pad A42: /Multibridge/CD31 -> /PerBus/D31
- J2 pad A44: /Multibridge/CD_~ADH -> /PerBus/~ADH
- J2 pad A46: /Multibridge/CD_~SS1 -> /PerBus/~SS1
- J2 pad A48: /Multibridge/CD_R/~W -> /PerBus/R/~W
- J2 pad A5: /Multibridge/CD_SCLK -> /PerBus/SER_CLK
- J2 pad A6: /Multibridge/CD_MOSI -> /PerBus/SER_MOSI
- J2 pad A7: /Multibridge/CD_MISO -> /PerBus/SER_MISO
- J2 pad B12: /Multibridge/CD0 -> /PerBus/D0
- J2 pad B14: /Multibridge/CD2 -> /PerBus/D2
- J2 pad B16: /Multibridge/CD4 -> /PerBus/D4
- J2 pad B18: /Multibridge/CD6 -> /PerBus/D6
- J2 pad B20: /Multibridge/CD8 -> /PerBus/D8
- J2 pad B22: /Multibridge/CD10 -> /PerBus/D10
- J2 pad B24: /Multibridge/CD12 -> /PerBus/D12
- J2 pad B26: /Multibridge/CD14 -> /PerBus/D14
- J2 pad B28: /Multibridge/CD16 -> /PerBus/D16
- J2 pad B30: /Multibridge/CD18 -> /PerBus/D18
- J2 pad B32: /Multibridge/CD20 -> /PerBus/D20
- J2 pad B34: /Multibridge/CD22 -> /PerBus/D22
- J2 pad B36: /Multibridge/CD24 -> /PerBus/D24
- J2 pad B38: /Multibridge/CD26 -> /PerBus/D26
- J2 pad B40: /Multibridge/CD28 -> /PerBus/D28
- J2 pad B42: /Multibridge/CD30 -> /PerBus/D30
- J2 pad B44: /Multibridge/CD_CLK -> /PerBus/CLK
- J2 pad B46: /Multibridge/CD_~ADL -> /PerBus/~ADL
- J3 pad A12: /Multibridge/CD1 -> /PerBus/D1
- J3 pad A14: /Multibridge/CD3 -> /PerBus/D3
- J3 pad A16: /Multibridge/CD5 -> /PerBus/D5
- J3 pad A18: /Multibridge/CD7 -> /PerBus/D7
- J3 pad A20: /Multibridge/CD9 -> /PerBus/D9
- J3 pad A22: /Multibridge/CD11 -> /PerBus/D11
- J3 pad A24: /Multibridge/CD13 -> /PerBus/D13
- J3 pad A26: /Multibridge/CD15 -> /PerBus/D15
- J3 pad A28: /Multibridge/CD17 -> /PerBus/D17
- J3 pad A30: /Multibridge/CD19 -> /PerBus/D19
- J3 pad A32: /Multibridge/CD21 -> /PerBus/D21
- J3 pad A34: /Multibridge/CD23 -> /PerBus/D23
- J3 pad A36: /Multibridge/CD25 -> /PerBus/D25
- J3 pad A38: /Multibridge/CD27 -> /PerBus/D27
- J3 pad A40: /Multibridge/CD29 -> /PerBus/D29
- J3 pad A42: /Multibridge/CD31 -> /PerBus/D31
- J3 pad A44: /Multibridge/CD_~ADH -> /PerBus/~ADH
- J3 pad A46: /Multibridge/CD_~SS2 -> /PerBus/~SS2
- J3 pad A48: /Multibridge/CD_R/~W -> /PerBus/R/~W
- J3 pad A5: /Multibridge/CD_SCLK -> /PerBus/SER_CLK
- J3 pad A6: /Multibridge/CD_MOSI -> /PerBus/SER_MOSI
- J3 pad A7: /Multibridge/CD_MISO -> /PerBus/SER_MISO
- J3 pad B12: /Multibridge/CD0 -> /PerBus/D0
- J3 pad B14: /Multibridge/CD2 -> /PerBus/D2
- J3 pad B16: /Multibridge/CD4 -> /PerBus/D4
- J3 pad B18: /Multibridge/CD6 -> /PerBus/D6
- J3 pad B20: /Multibridge/CD8 -> /PerBus/D8
- J3 pad B22: /Multibridge/CD10 -> /PerBus/D10
- J3 pad B24: /Multibridge/CD12 -> /PerBus/D12
- J3 pad B26: /Multibridge/CD14 -> /PerBus/D14
- J3 pad B28: /Multibridge/CD16 -> /PerBus/D16
- J3 pad B30: /Multibridge/CD18 -> /PerBus/D18
- J3 pad B32: /Multibridge/CD20 -> /PerBus/D20
- J3 pad B34: /Multibridge/CD22 -> /PerBus/D22
- J3 pad B36: /Multibridge/CD24 -> /PerBus/D24
- J3 pad B38: /Multibridge/CD26 -> /PerBus/D26
- J3 pad B40: /Multibridge/CD28 -> /PerBus/D28
- J3 pad B42: /Multibridge/CD30 -> /PerBus/D30
- J3 pad B44: /Multibridge/CD_CLK -> /PerBus/CLK
- J3 pad B46: /Multibridge/CD_~ADL -> /PerBus/~ADL
- J4 pad A12: /Multibridge/CD1 -> /PerBus/D1
- J4 pad A14: /Multibridge/CD3 -> /PerBus/D3
- J4 pad A16: /Multibridge/CD5 -> /PerBus/D5
- J4 pad A18: /Multibridge/CD7 -> /PerBus/D7
- J4 pad A20: /Multibridge/CD9 -> /PerBus/D9
- J4 pad A22: /Multibridge/CD11 -> /PerBus/D11
- J4 pad A24: /Multibridge/CD13 -> /PerBus/D13
- J4 pad A26: /Multibridge/CD15 -> /PerBus/D15
- J4 pad A28: /Multibridge/CD17 -> /PerBus/D17
- J4 pad A30: /Multibridge/CD19 -> /PerBus/D19
- J4 pad A32: /Multibridge/CD21 -> /PerBus/D21
- J4 pad A34: /Multibridge/CD23 -> /PerBus/D23
- J4 pad A36: /Multibridge/CD25 -> /PerBus/D25
- J4 pad A38: /Multibridge/CD27 -> /PerBus/D27
- J4 pad A40: /Multibridge/CD29 -> /PerBus/D29
- J4 pad A42: /Multibridge/CD31 -> /PerBus/D31
- J4 pad A44: /Multibridge/CD_~ADH -> /PerBus/~ADH
- J4 pad A46: /Multibridge/CD_~SS3 -> /PerBus/~SS3
- J4 pad A48: /Multibridge/CD_R/~W -> /PerBus/R/~W
- J4 pad A5: /Multibridge/CD_SCLK -> /PerBus/SER_CLK
- J4 pad A6: /Multibridge/CD_MOSI -> /PerBus/SER_MOSI
- J4 pad A7: /Multibridge/CD_MISO -> /PerBus/SER_MISO
- J4 pad B12: /Multibridge/CD0 -> /PerBus/D0
- J4 pad B14: /Multibridge/CD2 -> /PerBus/D2
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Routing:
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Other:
- net class Default: clearance 0.2 -> 0.125; trace_width 0.2 -> 0.125; via_dia 0.8 -> 0.5; via_drill 0.4 -> 0.2
- rule trace_clearance: 0.2 -> 0.125

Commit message: Begin implementing PCI
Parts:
- removed EC1: ATSAM4E16CA-AU, IPC7351-Nominal:QFP50P1600X1600X160-100
- removed J1, J2, J3, J4: CONN-10018783-10202TLF-PCIEx8, conn-fci:CONN-10018783-10202TLF-PCIEx8-FCI
- added LIMB1: ATSAME70NnnA-AN, IPC7351-Nominal:QFP50P1600X1600X160-100, F.Cu at (80.0, 25.0)
- added PCI0: CONN-5145154-1-PCI, conn-te:5145154-1, F.Cu at (139.4, 30.0)
- added PCI1: CONN-5145154-1-PCI, conn-te:5145154-1, F.Cu at (159.7, 30.0)
- added PCI2: CONN-5145154-1-PCI, conn-te:5145154-1, F.Cu at (119.0, 30.0)
- added PCI3: CONN-5145154-1-PCI, conn-te:5145154-1, F.Cu at (180.0, 30.0)
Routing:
- net /PerBus/D0: track 133.6 -> 0.00 mm, vias 1 -> 0
- net /PerBus/D2: track 130.3 -> 0.00 mm, vias 1 -> 0
- net /PerBus/D4: track 127.8 -> 0.00 mm, vias 1 -> 0
- net /PerBus/D1: track 127.5 -> 0.00 mm, vias 1 -> 0
- net (no net): track 179.3 -> 52.3 mm
- net /PerBus/D6: track 126.2 -> 0.00 mm, vias 1 -> 0
- net /PerBus/D3: track 125.1 -> 0.00 mm, vias 1 -> 0
- net /PerBus/D8: track 124.0 -> 0.00 mm, vias 1 -> 0
- net /PerBus/D5: track 122.5 -> 0.00 mm, vias 1 -> 0
- net /PerBus/D10: track 121.7 -> 0.00 mm, vias 1 -> 0
- net /PerBus/D7: track 120.9 -> 0.00 mm, vias 1 -> 0
- net /PerBus/D12: track 118.9 -> 0.00 mm, vias 1 -> 0
- net /PerBus/D9: track 118.5 -> 0.00 mm, vias 1 -> 0
- net /PerBus/D14: track 116.7 -> 0.00 mm, vias 1 -> 0
- net /PerBus/D11: track 116.7 -> 0.00 mm, vias 1 -> 0
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
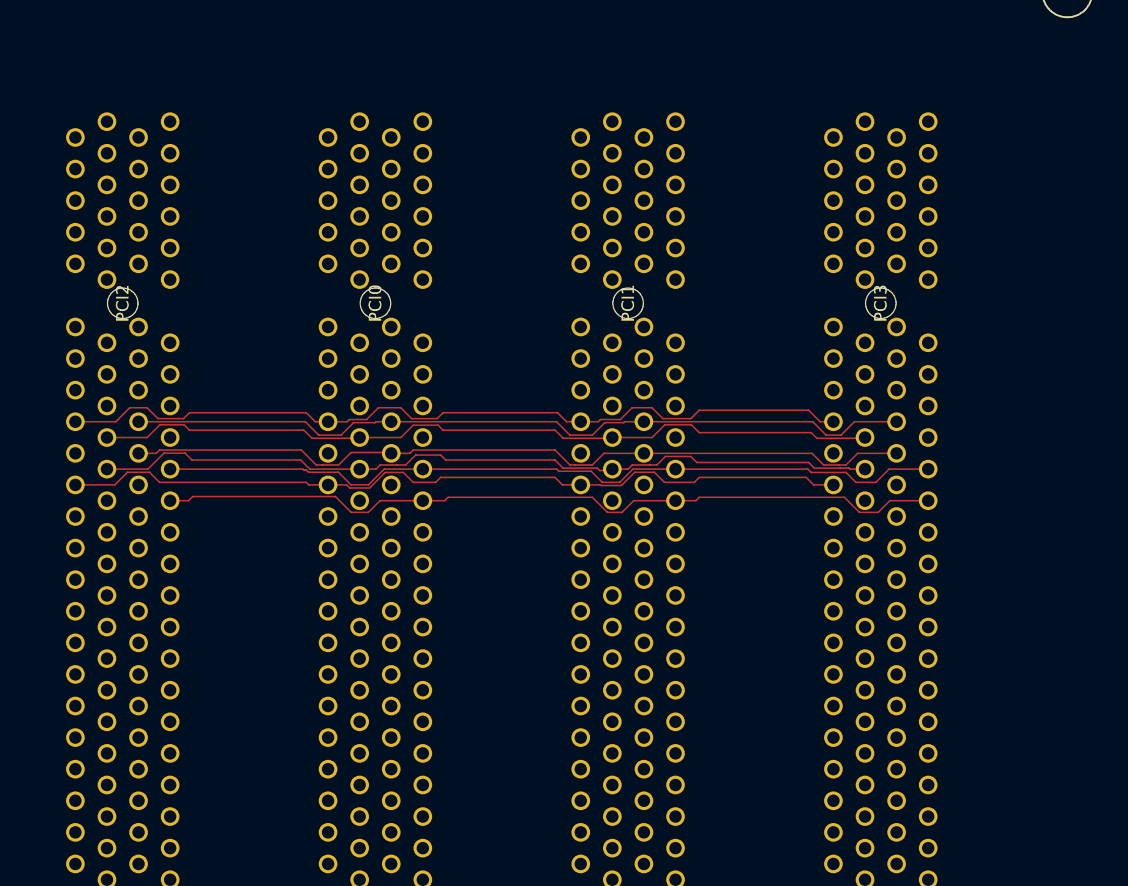
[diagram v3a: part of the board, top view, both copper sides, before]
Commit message: PCI bus decoupling
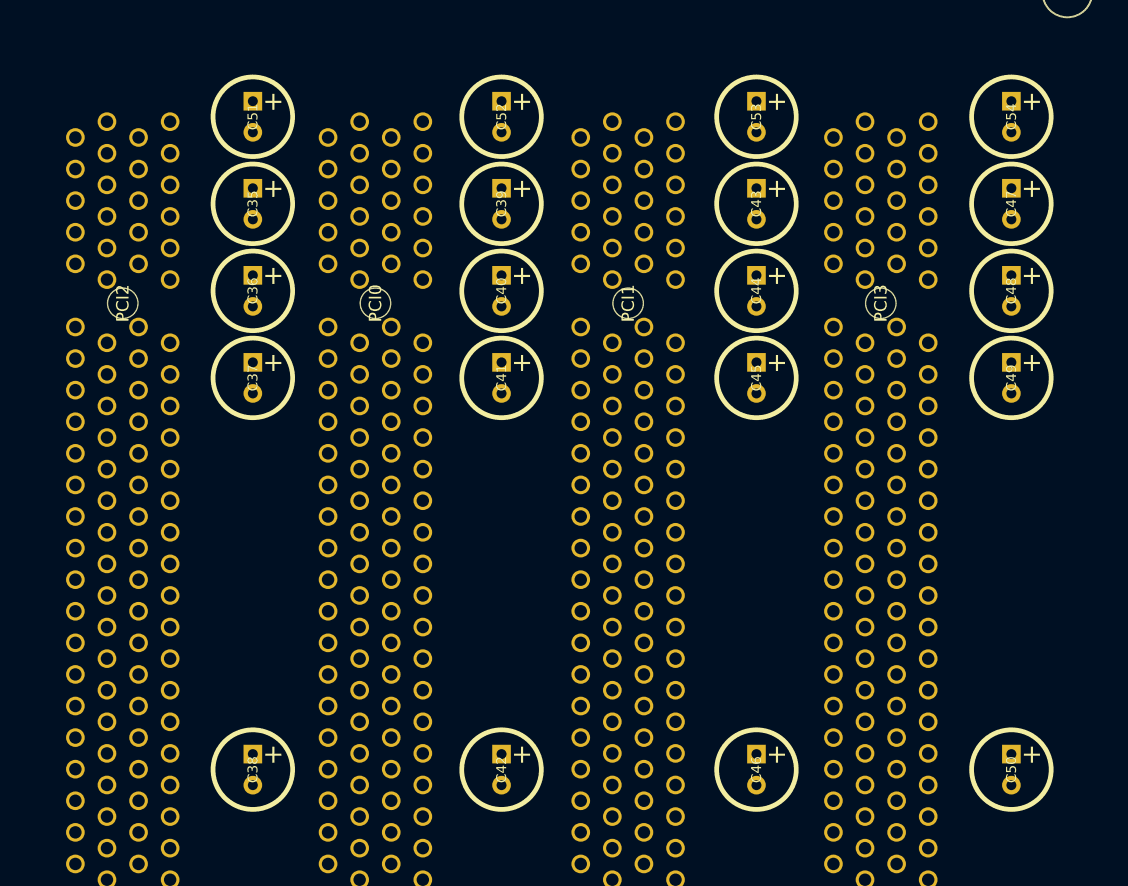
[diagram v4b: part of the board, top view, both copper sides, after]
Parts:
- added C35: 47u, pth-passive:C-ALUM-6.3mm, F.Cu at (129.5, 22.0)
- added C36: 220u, pth-passive:C-ALUM-6.3mm, F.Cu at (129.5, 29.0)
- added C37: 220u, pth-passive:C-ALUM-6.3mm, F.Cu at (129.5, 36.0)
- added C38: 220u, pth-passive:C-ALUM-6.3mm, F.Cu at (129.5, 67.5)
- added C39: 47u, pth-passive:C-ALUM-6.3mm, F.Cu at (149.5, 22.0)
- added C40: 220u, pth-passive:C-ALUM-6.3mm, F.Cu at (149.5, 29.0)
- added C41: 220u, pth-passive:C-ALUM-6.3mm, F.Cu at (149.5, 36.0)
- added C42: 220u, pth-passive:C-ALUM-6.3mm, F.Cu at (149.5, 67.5)
- added C43: 47u, pth-passive:C-ALUM-6.3mm, F.Cu at (170.0, 22.0)
- added C44: 220u, pth-passive:C-ALUM-6.3mm, F.Cu at (170.0, 29.0)
- added C45: 220u, pth-passive:C-ALUM-6.3mm, F.Cu at (170.0, 36.0)
- added C46: 220u, pth-passive:C-ALUM-6.3mm, F.Cu at (170.0, 67.5)
- added C47: 47u, pth-passive:C-ALUM-6.3mm, F.Cu at (190.5, 22.0)
- added C48: 220u, pth-passive:C-ALUM-6.3mm, F.Cu at (190.5, 29.0)
- added C49: 220u, pth-passive:C-ALUM-6.3mm, F.Cu at (190.5, 36.0)
- added C50: 220u, pth-passive:C-ALUM-6.3mm, F.Cu at (190.5, 67.5)
- added C51: 47u, pth-passive:C-ALUM-6.3mm, F.Cu at (129.5, 15.0)
- added C52: 47u, pth-passive:C-ALUM-6.3mm, F.Cu at (149.5, 15.0)
- added C53: 47u, pth-passive:C-ALUM-6.3mm, F.Cu at (170.0, 15.0)
- added C54: 47u, pth-passive:C-ALUM-6.3mm, F.Cu at (190.5, 15.0)
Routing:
- net /PerBus/PCI_AD31: track 65.1 -> 0.00 mm
- net /PerBus/PCI_AD25: track 64.4 -> 0.00 mm
- net /PerBus/PCI_AD24: track 64.0 -> 0.00 mm
- net /PerBus/PCI_AD27: track 63.9 -> 0.00 mm
- net /PerBus/PCI_AD28: track 63.8 -> 0.00 mm
- net /PerBus/PCI_AD26: track 63.8 -> 0.00 mm
- net /PerBus/PCI_AD30: track 63.6 -> 0.00 mm
- net /PerBus/PCI_AD29: track 63.6 -> 0.00 mm
